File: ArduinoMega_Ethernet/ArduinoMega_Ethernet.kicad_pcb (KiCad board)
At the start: 2 copper layers, 101.6 x 53.3 mm, 120 parts, among them J1 RJ45_Amphenol_RJMG1BD3B8K1ANR, J11 Micro_SD_Card_Det_Hirose_DM3AT, J2 SD_DET_JUMP, J3 IMU_INT1_JUMP, J4 IMU_INT2_JUMP, J5 ETHER_INT_JUMP, J6 RTC_MFP_JUMP, J7 EXT_3V3_I2C, J9 PROGRAM_POWER_USBC, SW1 SW_Push, U1 ATmega2560-16A, U10 TXS0108EPW, U2 CH340C, U3 ISM330DHCX, U4 W5500, U5 AP63205WU, U6 AP63203WU, U7 SE050C2HQ1, U8 AP22804AW5, U9 MCP7940N-xST, Y1 16Mhz, Y2 25Mhz, Y3 32.768kHz

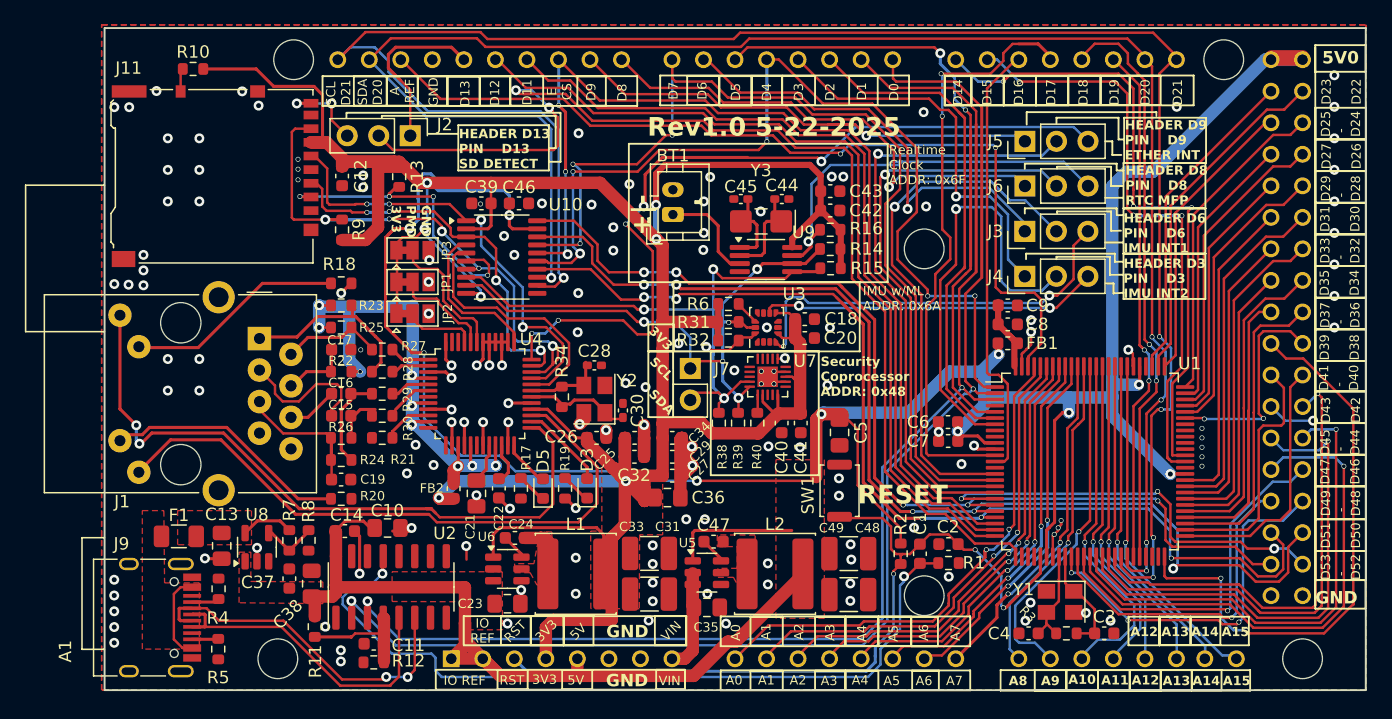
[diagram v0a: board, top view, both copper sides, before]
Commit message: swap sd card mosi miso
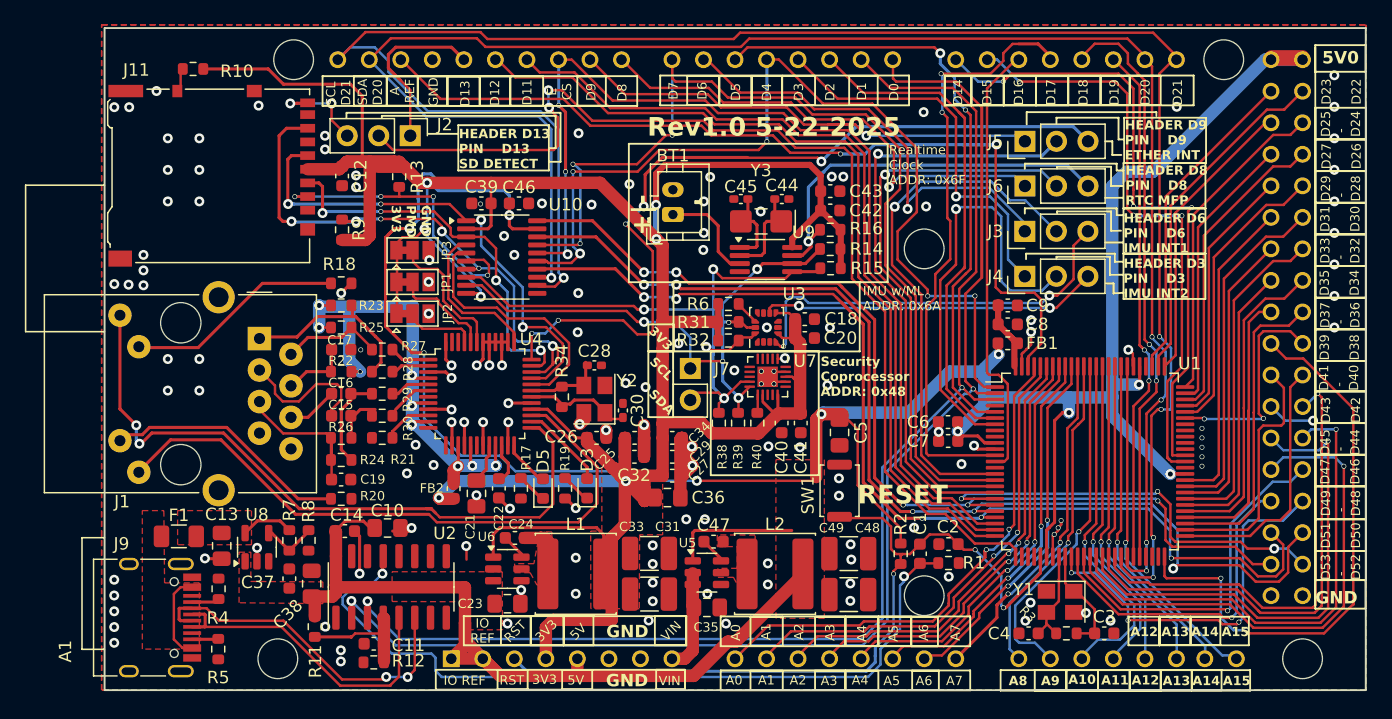
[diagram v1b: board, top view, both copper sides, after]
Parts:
- moved J11 0.27 mm to (111.0, 75.4)
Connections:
- J11 pad 4: GND -> +3V3
- J11 pad 6: +3V3 -> GND
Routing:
- net /PIN_D13: track 91.4 -> 86.0 mm
- net /PWRandPRG/ETHERNET_SCLK: track 35.8 -> 40.1 mm
- net /PWRandPRG/ETHERNET_MISO: track 49.1 -> 45.4 mm, vias 5 -> 6
- net /MCU_AREF_IN: track 72.6 -> 75.3 mm
- net GND: track 68.7 -> 67.1 mm, vias 150 -> 146
- net /SD_DET: track 7.07 -> 8.12 mm
- net Net-(JP2-C): track 6.40 -> 5.43 mm
- net Net-(U9-X1): track 6.66 -> 5.79 mm
- net Net-(U4-XI/CLKIN): track 8.57 -> 7.77 mm
- net /PIN_D51: track 89.5 -> 88.7 mm
- net /PIN_D52: track 83.3 -> 82.5 mm
- net /PWRandPRG/ETHERNET_MOSI: track 31.8 -> 32.6 mm
- net Net-(U9-X2): track 7.84 -> 7.11 mm
- net Net-(J1-RCT): track 12.7 -> 12.0 mm
- net Net-(J1-LEDY_K): track 19.8 -> 19.1 mm
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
